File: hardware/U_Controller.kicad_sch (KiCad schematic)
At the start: 5 parts, among them J4 USB_C_Receptacle_USB2.0_14P, U4 STM32C031K6Tx, U5 STM32C071RBT6

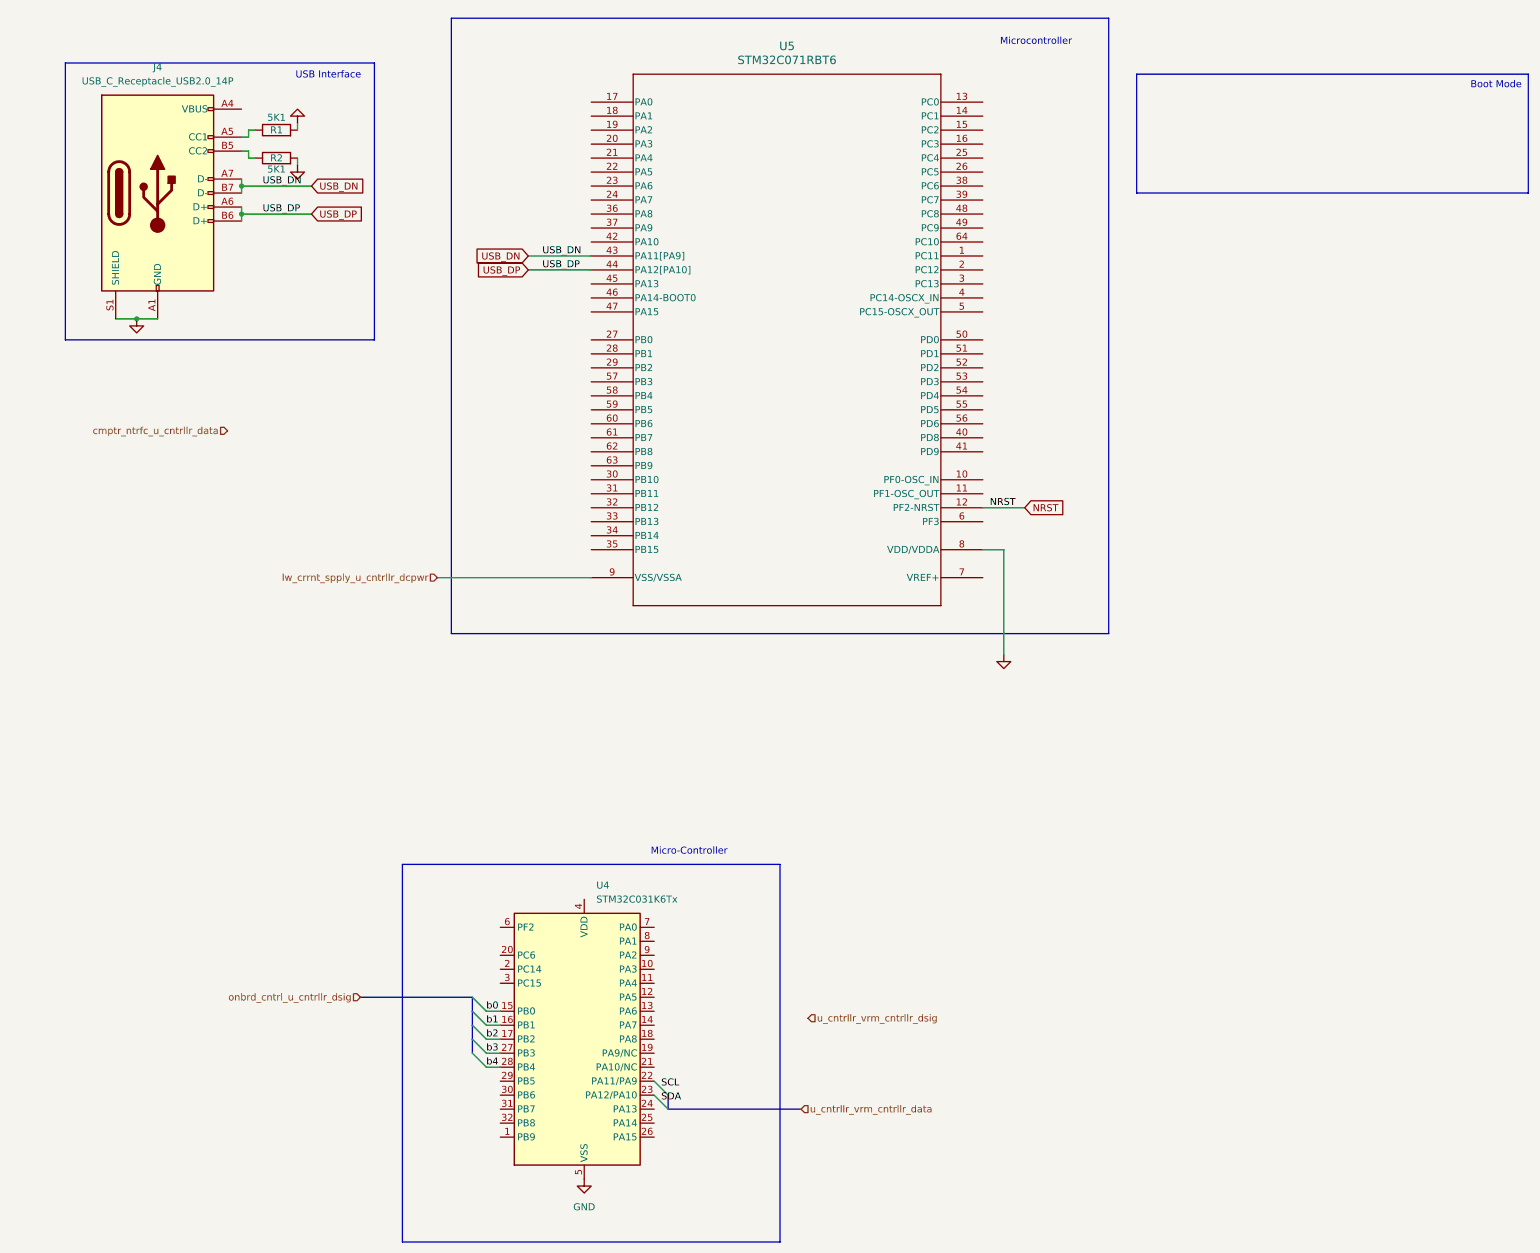
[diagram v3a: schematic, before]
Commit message: feat(schematic): Boot Mode Configuration
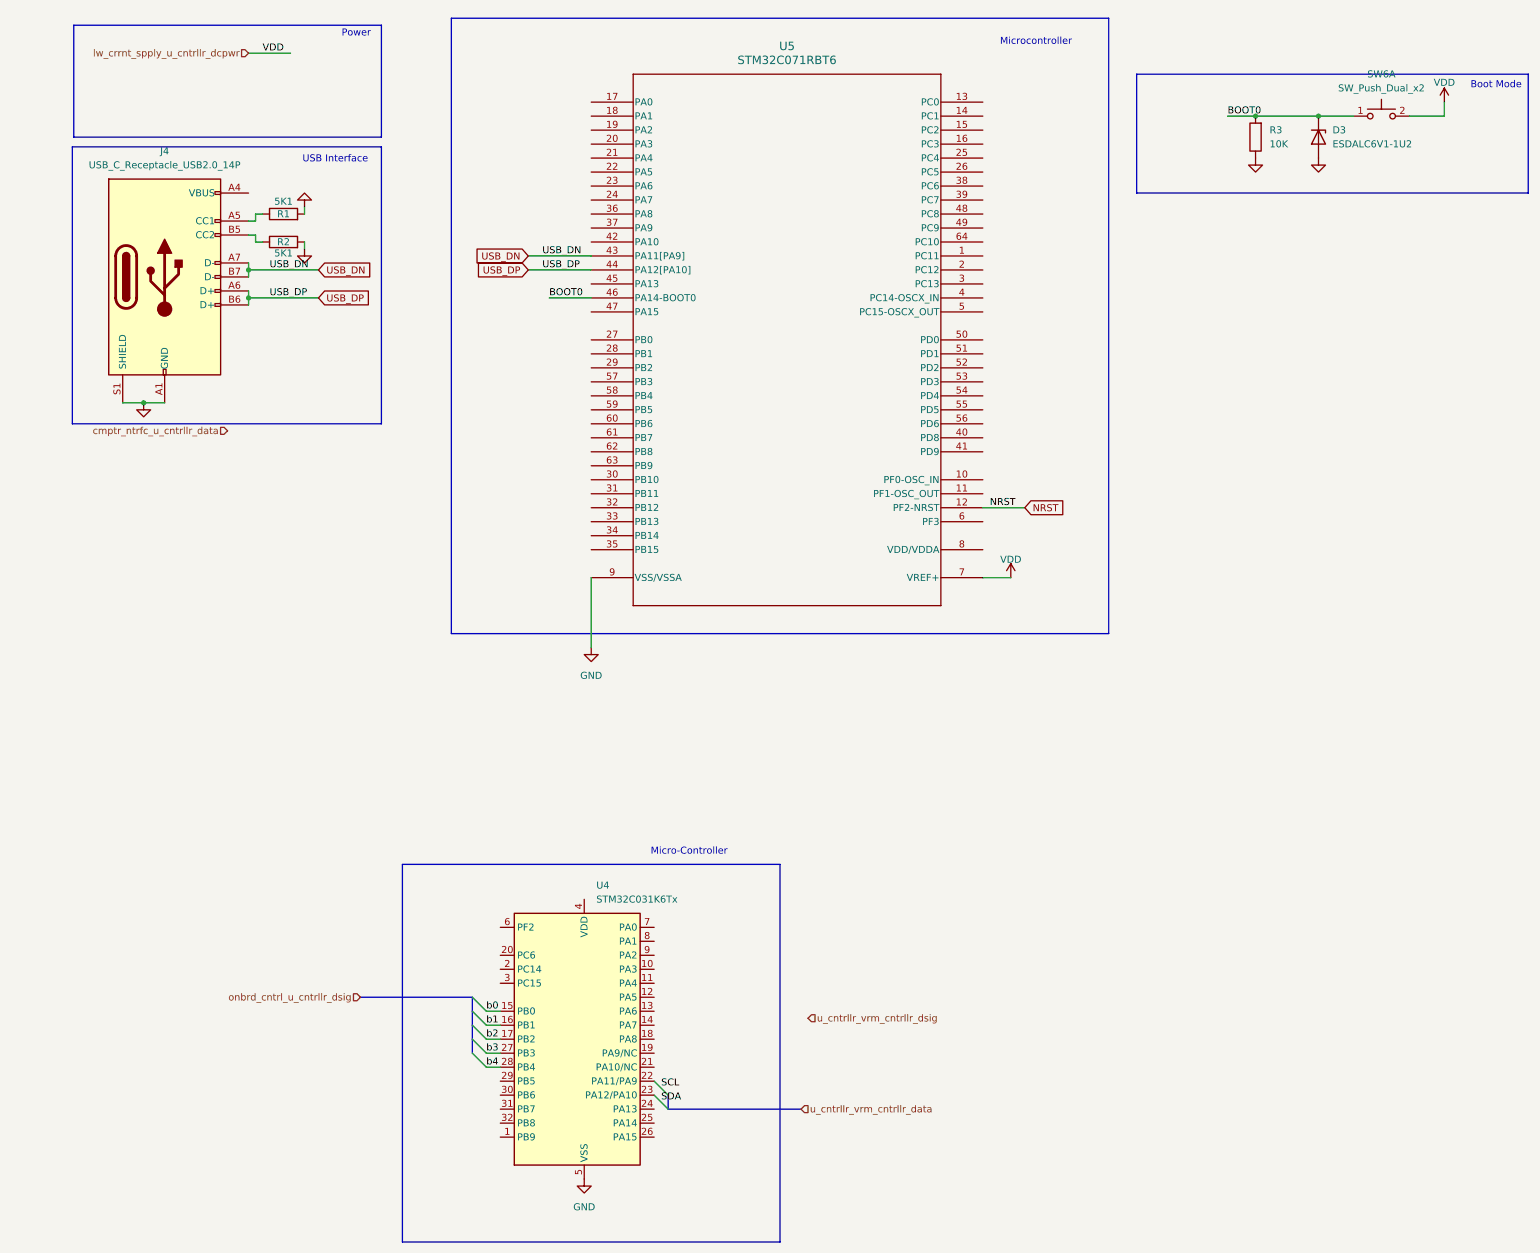
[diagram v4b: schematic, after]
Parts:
- added D3: ESDALC6V1-1U2, symbol Device:D_Zener
- added R3: 10K, symbol Device:R
- added SW6: SW_Push_Dual_x2, symbol Switch:SW_Push_Dual_x2
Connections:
- net lw_crrnt_spply_u_cntrllr_dcpwr is gone; now on net GND: U5.9 (VSS/VSSA)
- net GND: now also D3.2 (A), R3.1; no longer U5.8 (VDD/VDDA)
- net BOOT0: now reaches U5.46 (PA14-BOOT0)
- net BOOT0: now also D3.1 (K), R3.2, SW6.1 (C)
- net VDD: now reaches U5.7 (VREF+)
- net VDD: now also SW6.2 (D)
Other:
- note added: "Power"
- moved on the sheet: J4, R1, R2

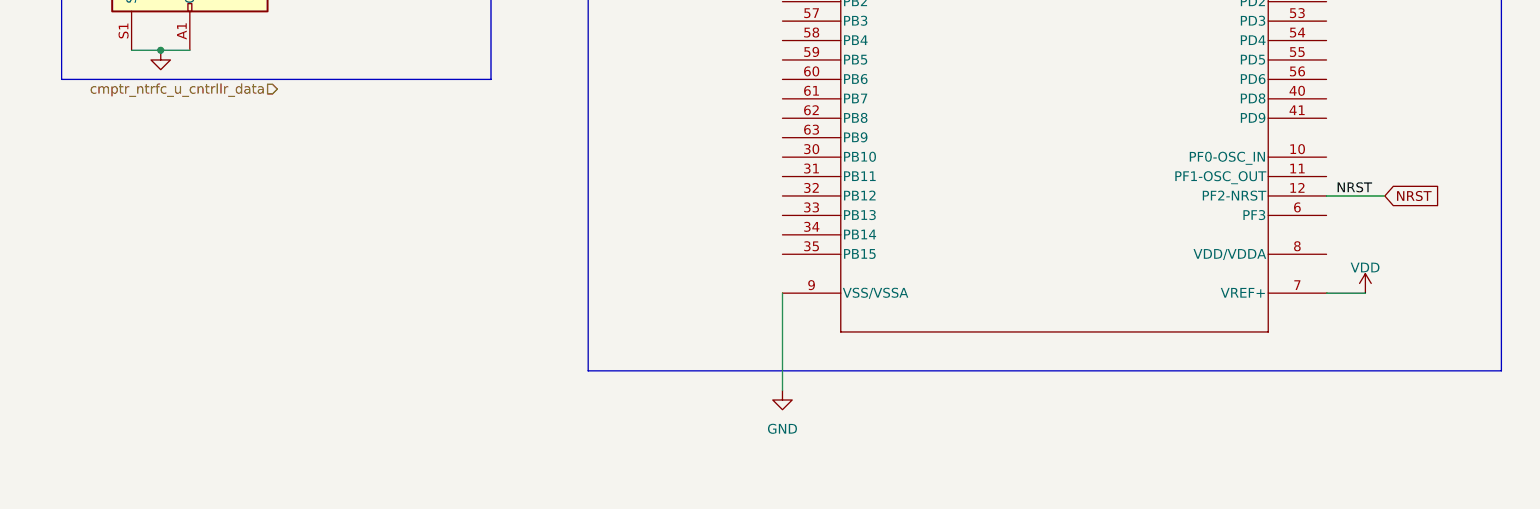
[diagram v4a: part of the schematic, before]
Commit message: feat(schematic): Microcontroller 48MHz oscillator
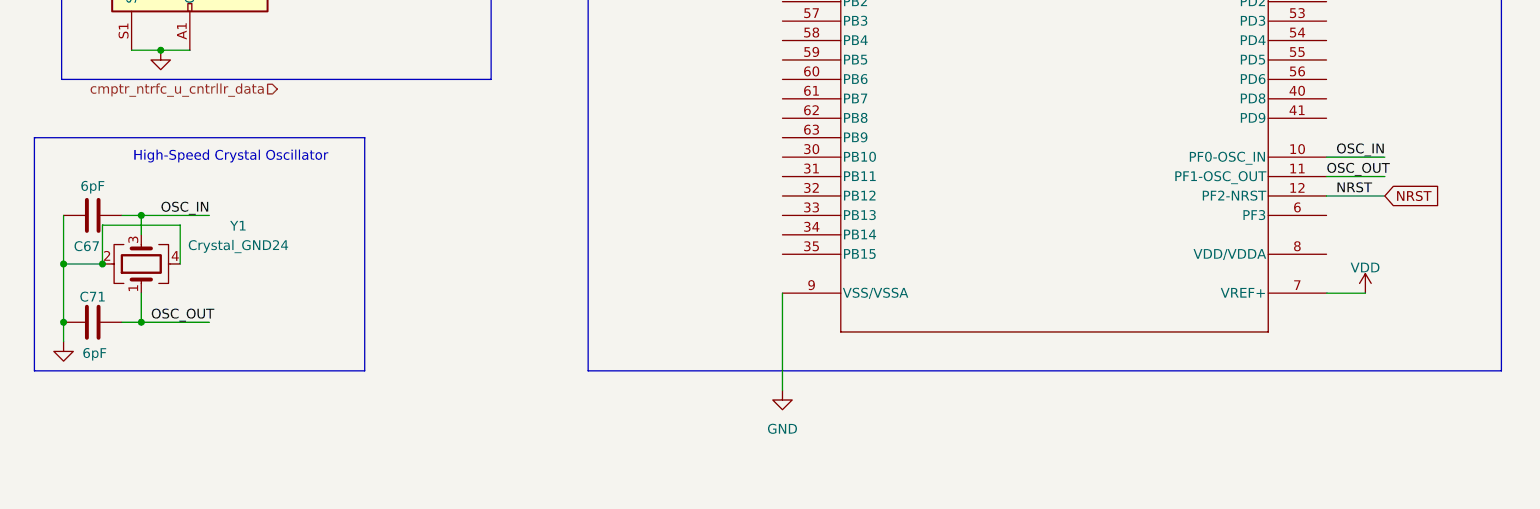
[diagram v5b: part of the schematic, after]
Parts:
- added C67, C71: 6pF, symbol Device:C
- added Y1: Crystal_GND24, symbol Device:Crystal_GND24
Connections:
- net GND: now also C67.1, C71.1, Y1.2, Y1.4
- net OSC_IN: now reaches U5.10 (PF0-OSC_IN)
- net OSC_IN: now also C67.2, Y1.3
- net OSC_OUT: now reaches U5.11 (PF1-OSC_OUT)
- net OSC_OUT: now also C71.2, Y1.1
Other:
- note added: "High-Speed Crystal Oscillator"

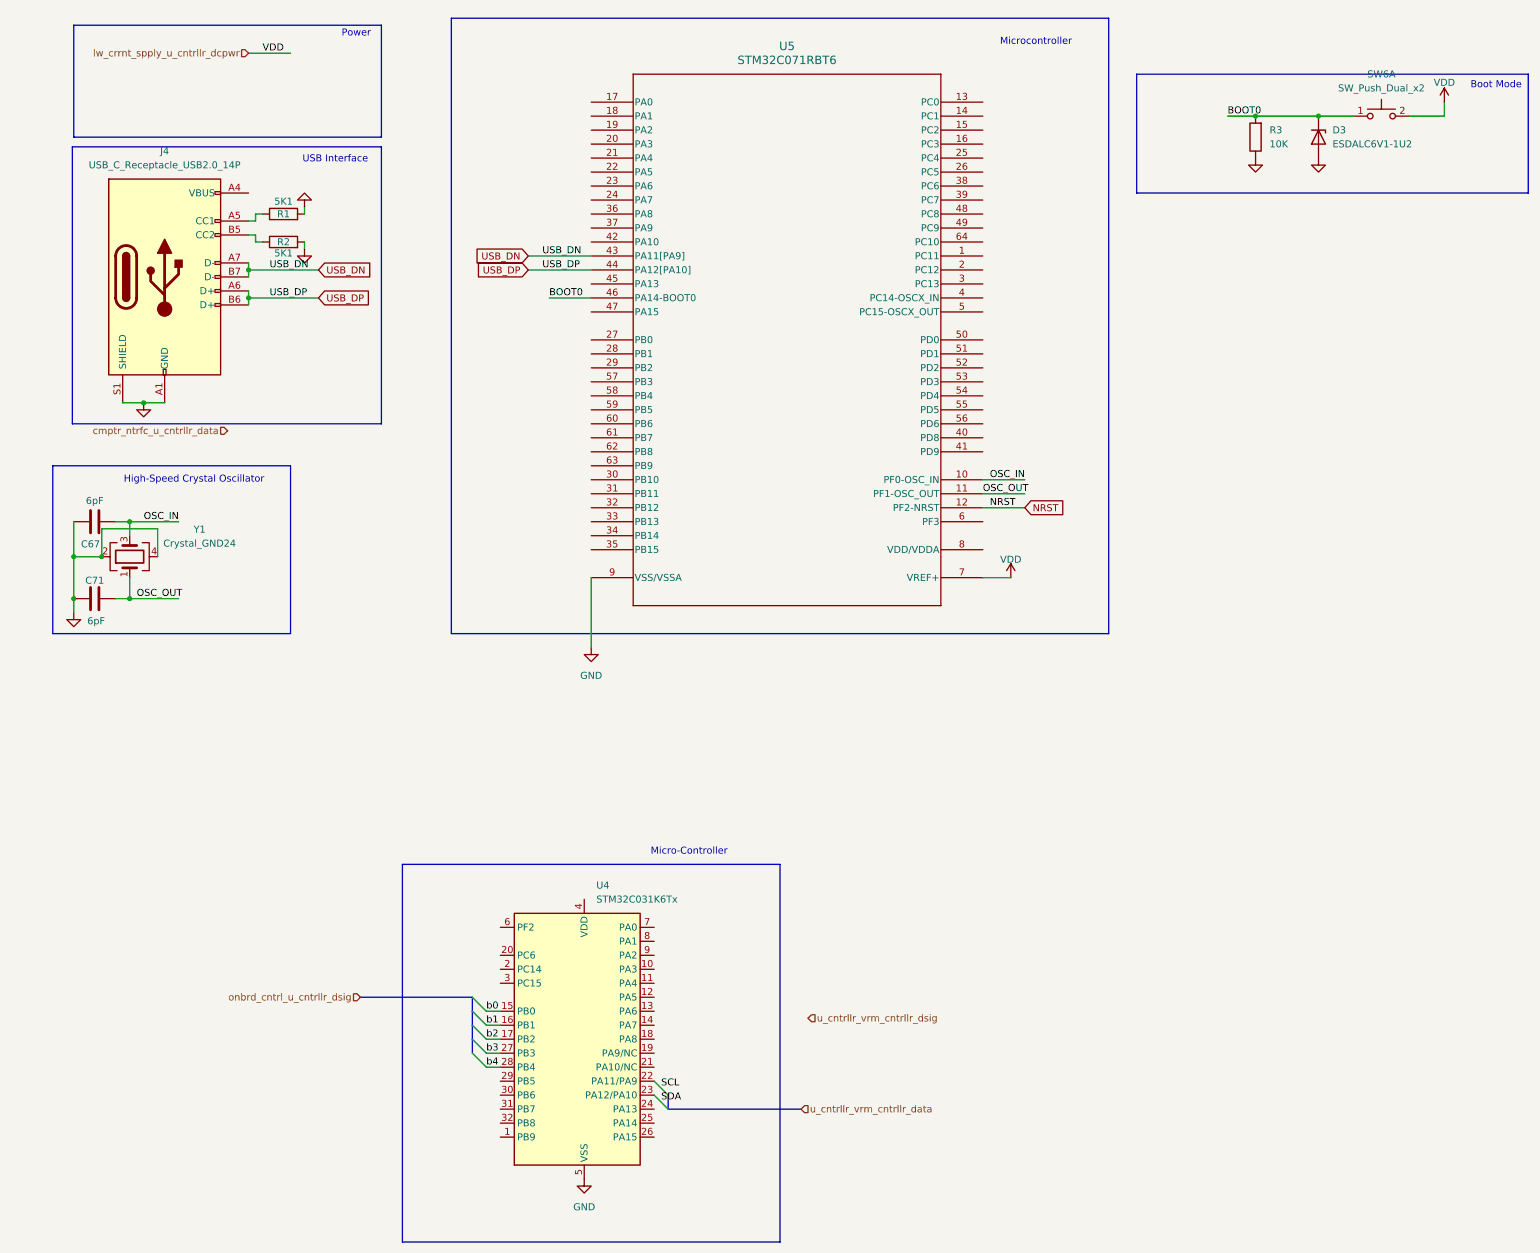
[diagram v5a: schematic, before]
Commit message: chore(schematic): Global Labels and Boot Mode Slider
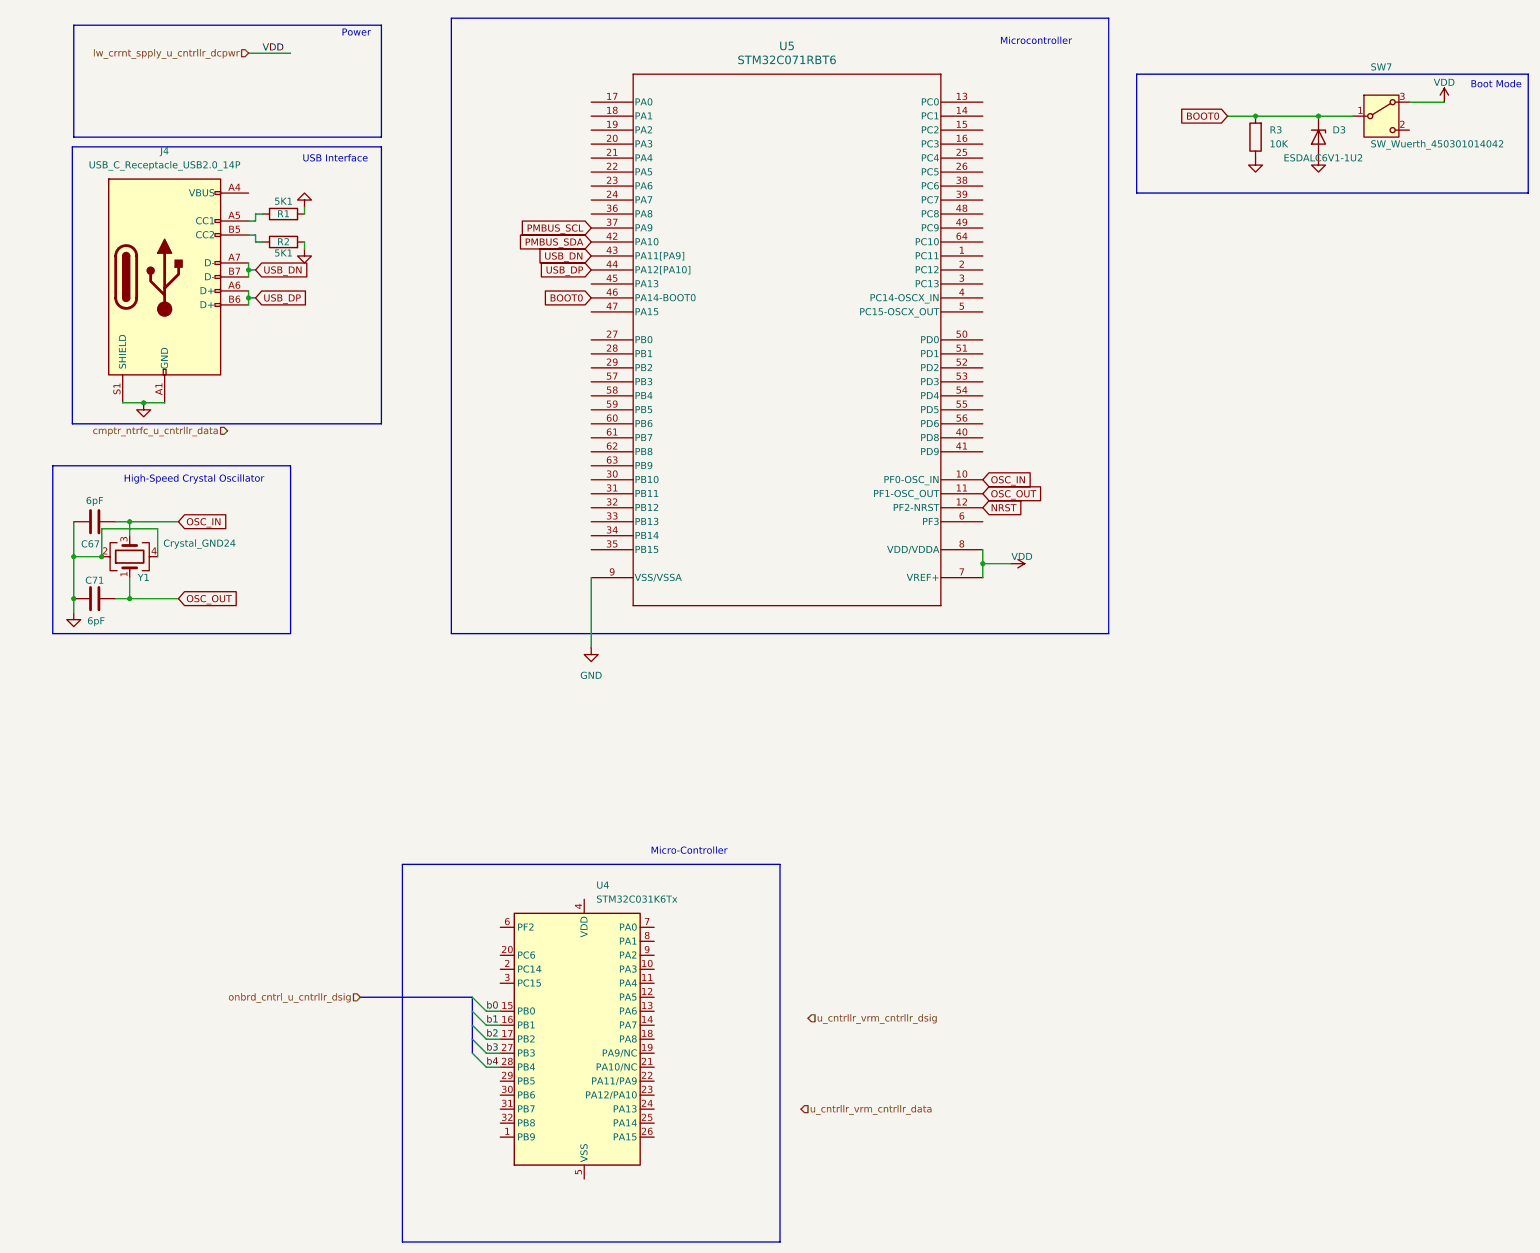
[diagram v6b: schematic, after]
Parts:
- removed SW6: SW_Push_Dual_x2, symbol Switch:SW_Push_Dual_x2
- added SW7: SW_Wuerth_450301014042, Button_Switch_THT:SW_Slide-03_Wuerth-WS-SLTV_10x2.5x6.4_P2.54mm, symbol Switch:SW_Wuerth_450301014042
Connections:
- net BOOT0: now also SW7.1 (B)
- net GND: no longer U4.5 (VSS)
- net VDD: now also U5.8 (VDD/VDDA), SW7.3 (A)
- net PMBUS_SCL: now reaches U5.37 (PA9)
- net PMBUS_SDA: now reaches U5.42 (PA10)
